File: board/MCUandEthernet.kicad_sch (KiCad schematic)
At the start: 3 parts, among them J1 RJ45_LED_Shielded, U15 Teensy4.1_DEV-16771

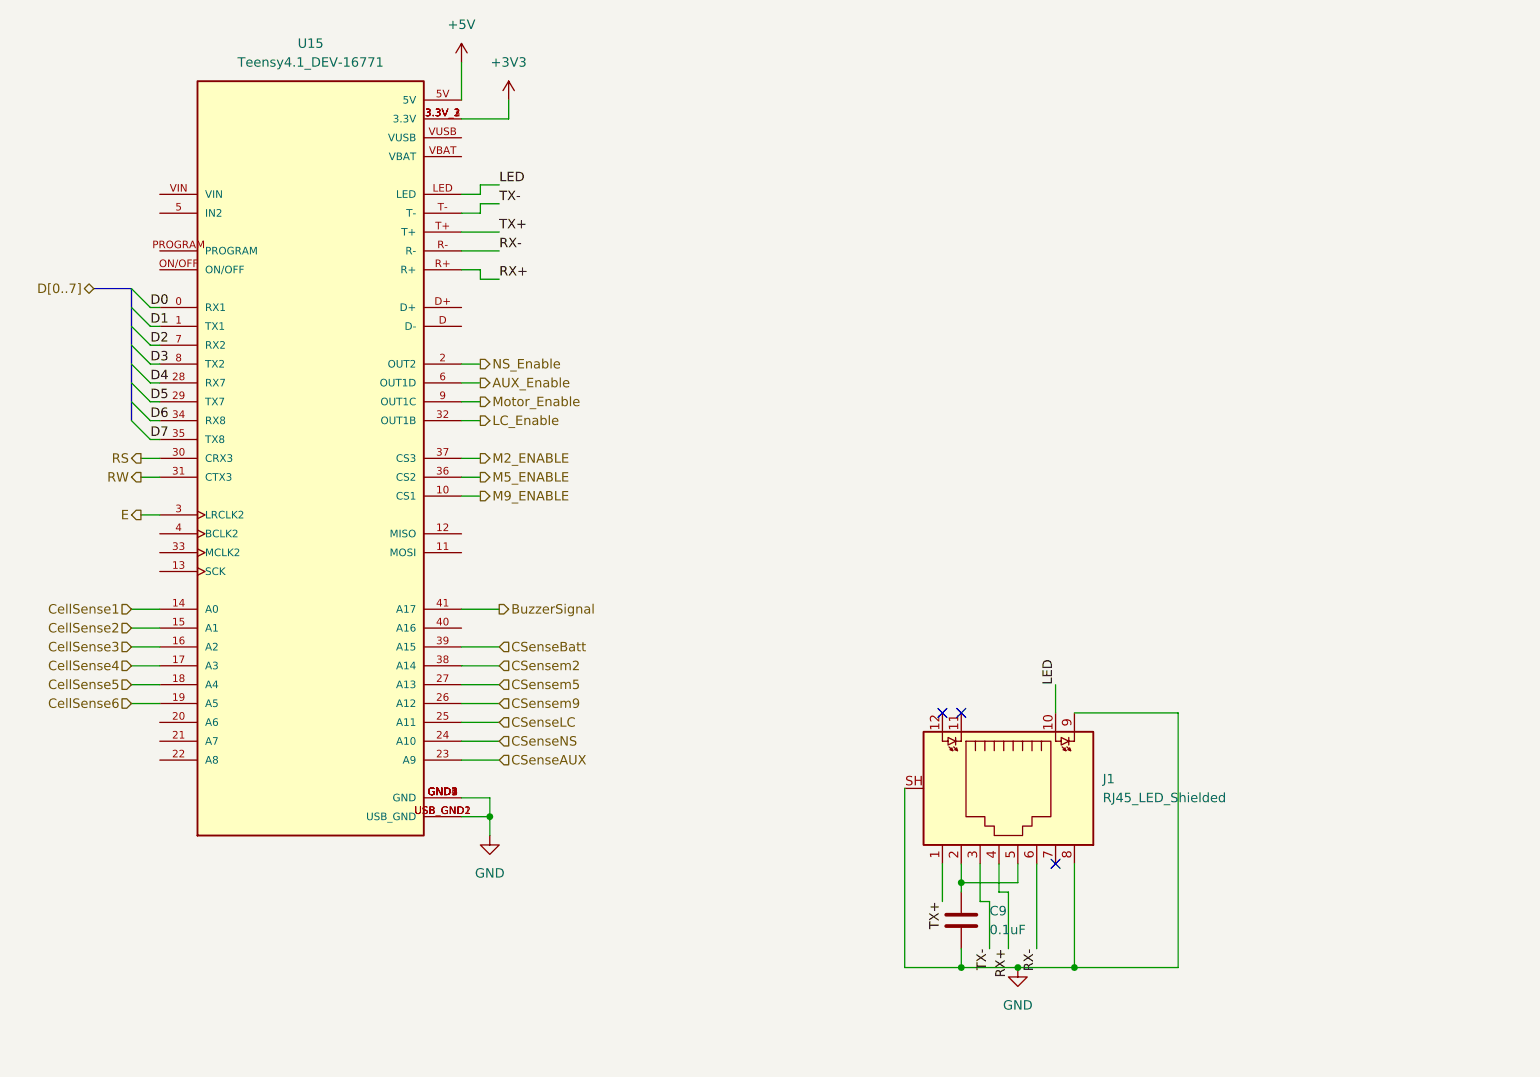
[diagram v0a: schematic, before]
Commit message: added fixes for schematic
redid op amp symbols
put Xs on teensy
Put andersons on current protection page
changed resistor value for buzzer
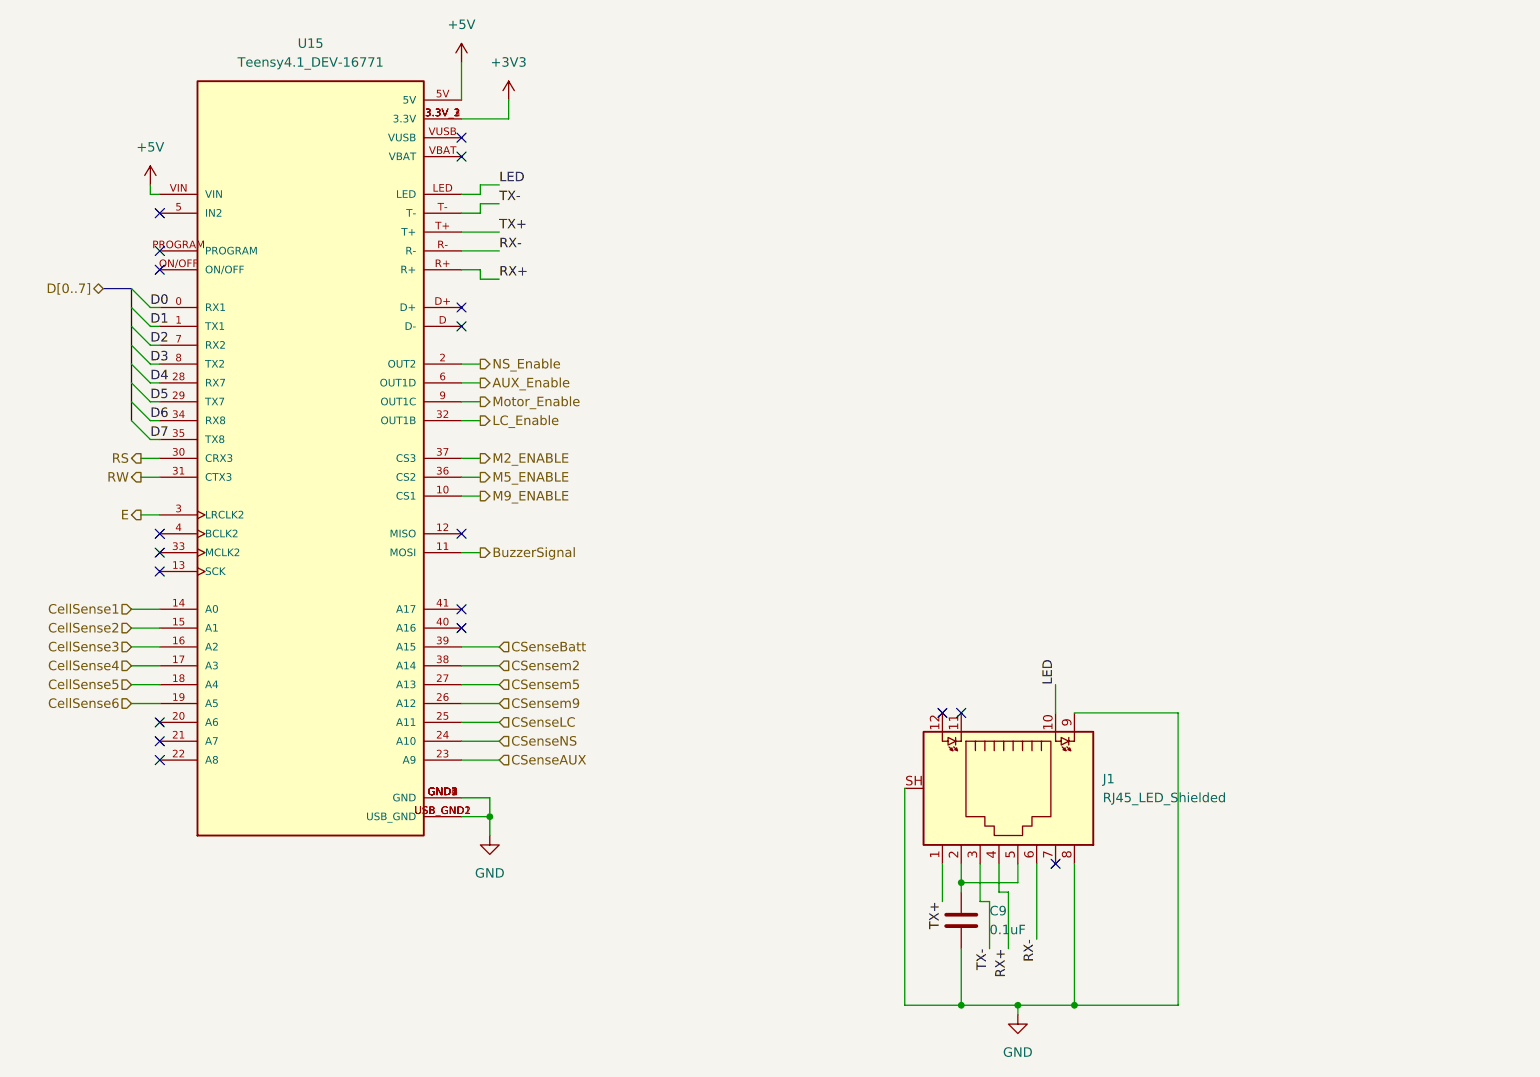
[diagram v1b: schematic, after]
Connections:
- net +5V: now also U15.VIN
- net BuzzerSignal: now also U15.11 (MOSI); no longer U15.41 (A17)
- no-connect marks 3 -> 19
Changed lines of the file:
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@@
 	)
 	(junction
-		(at 135.89 162.56)
+		(at 151.13 167.64)
+		(diameter 0)
+		(color 0 0 0 0)
+	)
+	(junction
+		(at 143.51 167.64)
 		(diameter 0)
 		(color 0 0 0 0)
@@
 	)
 	(junction
-		(at 151.13 162.56)
+		(at 135.89 167.64)
 		(diameter 0)
 		(color 0 0 0 0)
 	)
-	(junction
-		(at 143.51 162.56)
-		(diameter 0)
-		(color 0 0 0 0)
-	)
 	(no_connect
 		(at 133.35 128.27)
 	)
 	(no_connect
+		(at 27.94 68.58)
+	)
+	(no_connect
+		(at 27.94 129.54)
+	)
+	(no_connect
+		(at 68.58 114.3)
+	)
+	(no_connect
+		(at 27.94 134.62)
+	)
+	(no_connect
+		(at 68.58 104.14)
+	)
+	(no_connect
 		(at 148.59 148.59)
 	)
 	(no_connect
+		(at 27.94 106.68)
+	)
+	(no_connect
+		(at 27.94 109.22)
+	)
+	(no_connect
+		(at 27.94 60.96)
+	)
+	(no_connect
+		(at 27.94 104.14)
+	)
+	(no_connect
+		(at 68.58 50.8)
+	)
+	(no_connect
 		(at 135.89 128.27)
+	)
+	(no_connect
+		(at 68.58 76.2)
+	)
+	(no_connect
+		(at 68.58 116.84)
+	)
+	(no_connect
+		(at 68.58 73.66)
+	)
+	(no_connect
+		(at 27.94 132.08)
+	)
+	(no_connect
+		(at 68.58 53.34)
+	)
+	(no_connect
+		(at 27.94 66.04)
 	)
 	(bus_entry
@@
 	(wire
 		(pts
-			(xy 128.27 162.56) (xy 135.89 162.56)
-		)
-		(stroke
-			(width 0)
-			(type default)
-		)
-	)
-	(wire
-		(pts
-			(xy 151.13 148.59) (xy 151.13 162.56)
+			(xy 128.27 167.64) (xy 135.89 167.64)
 		)
 		(stroke
@@
 	(wire
 		(pts
-			(xy 165.1 128.27) (xy 165.1 162.56)
+			(xy 165.1 128.27) (xy 165.1 167.64)
 		)
 		(stroke
@@
 	(wire
 		(pts
+			(xy 26.67 58.42) (xy 27.94 58.42)
+		)
+		(stroke
+			(width 0)
+			(type default)
+		)
+	)
+	(wire
+		(pts
 			(xy 26.67 88.9) (xy 27.94 88.9)
 		)
@@
 	(wire
 		(pts
+			(xy 151.13 148.59) (xy 151.13 167.64)
+		)
+		(stroke
+			(width 0)
+			(type default)
+		)
+	)
+	(wire
+		(pts
 			(xy 24.13 127) (xy 27.94 127)
 		)
@@
 	(wire
 		(pts
-			(xy 68.58 114.3) (xy 73.66 114.3)
-		)
-		(stroke
-			(width 0)
-			(type default)
-		)
-	)
-	(wire
-		(pts
-			(xy 165.1 162.56) (xy 151.13 162.56)
+			(xy 165.1 167.64) (xy 151.13 167.64)
 		)
 		(stroke
@@
 	(wire
 		(pts
+			(xy 143.51 168.91) (xy 143.51 167.64)
+		)
+		(stroke
+			(width 0)
+			(type default)
+		)
+	)
+	(wire
+		(pts
 			(xy 138.43 153.67) (xy 138.43 148.59)
 		)
@@
 	(bus
 		(pts
-			(xy 19.05 71.12) (xy 24.13 71.12)
+			(xy 20.32 71.12) (xy 24.13 71.12)
+		)
+		(stroke
+			(width 0)
+			(type default)
+		)
+	)
+	(wire
+		(pts
+			(xy 26.67 57.15) (xy 26.67 58.42)
 		)
 		(stroke
@@
 	(wire
 		(pts
-			(xy 135.89 162.56) (xy 143.51 162.56)
+			(xy 135.89 167.64) (xy 143.51 167.64)
 		)
 		(stroke
@@
 	(wire
 		(pts
-			(xy 128.27 138.43) (xy 128.27 162.56)
+			(xy 128.27 138.43) (xy 128.27 167.64)
 		)
 		(stroke
@@
 	(wire
 		(pts
-			(xy 146.05 148.59) (xy 146.05 160.02)
+			(xy 146.05 148.59) (xy 146.05 158.75)
 		)
 		(stroke
@@
 	(wire
 		(pts
-			(xy 151.13 162.56) (xy 143.51 162.56)
+			(xy 151.13 167.64) (xy 143.51 167.64)
 		)
 		(stroke
@@
 	(wire
 		(pts
+			(xy 71.12 106.68) (xy 68.58 106.68)
+		)
+		(stroke
+			(width 0)
+			(type default)
+		)
+	)
+	(wire
+		(pts
 			(xy 71.12 93.98) (xy 68.58 93.98)
 		)
@@
 	(wire
 		(pts
-			(xy 135.89 160.02) (xy 135.89 162.56)
+			(xy 135.89 160.02) (xy 135.89 167.64)
 		)
 		(stroke
@@
 	)
 	(label "RX-"
-		(at 146.05 160.02 270)
+		(at 146.05 158.75 270)
 		(effects
 			(font
@@
 	(hierarchical_label "BuzzerSignal"
 		(shape output)
-		(at 73.66 114.3 0)
+		(at 71.12 106.68 0)
 		(effects
 			(font
@@
 	(hierarchical_label "D[0..7]"
 		(shape bidirectional)
-		(at 19.05 71.12 180)
+		(at 20.32 71.12 180)
 		(effects
 			(font
@@
 			)
 			(justify left)
+		)
+	)
+	(symbol
+		(lib_id "power:+5V")
+		(at 26.67 57.15 0)
+		(unit 1)
+		(exclude_from_sim no)
+		(in_bom yes)
+		(on_board yes)
+		(dnp no)
+		(fields_autoplaced yes)
+		(property "Reference" "#PWR091"
+			(at 26.67 60.96 0)
+			(effects
+				(font
+					(size 1.27 1.27)
+				)
+				(hide yes)
+			)
+		)
+		(property "Value" "+5V"
+			(at 26.67 52.07 0)
+			(effects
+				(font
+					(size 1.27 1.27)
+				)
+			)
+		)
+		(property "Footprint" ""
+			(at 26.67 57.15 0)
+			(effects
+				(font
+					(size 1.27 1.27)
+				)
+				(hide yes)
+			)
+		)
+		(property "Datasheet" ""
+			(at 26.67 57.15 0)
+			(effects
+				(font
+					(size 1.27 1.27)
+				)
+				(hide yes)
+			)
+		)
+		(property "Description" "Power symbol creates a global label with name \"+5V\""
+			(at 26.67 57.15 0)
+			(effects
+				(font
+					(size 1.27 1.27)
+				)
+				(hide yes)
+			)
+		)
+		(pin "1"
+		)
+		(instances
+			(project "PowerManagementBoard"
+				(path "/7eaa639d-7062-45e7-be05-1c2855431307/4dc475e3-8611-4a67-a903-307f734d4f8b"
+					(reference "#PWR091")
+					(unit 1)
+				)
+			)
 		)
 	)
@@
 	(symbol
 		(lib_id "power:GND")
-		(at 143.51 162.56 0)
+		(at 143.51 168.91 0)
 		(unit 1)
 		(exclude_from_sim no)
@@
 		(fields_autoplaced yes)
 		(property "Reference" "#PWR041"
+			(at 143.51 175.26 0)
+			(effects
+				(font
+					(size 1.27 1.27)
+				)
+				(hide yes)
+			)
+		)
+		(property "Value" "GND"
+			(at 143.51 173.99 0)
+			(effects
+				(font
+					(size 1.27 1.27)
+				)
+			)
+		)
+		(property "Footprint" ""
 			(at 143.51 168.91 0)
 			(effects
@@
 			)
 		)
-		(property "Value" "GND"
-			(at 143.51 167.64 0)
+		(property "Datasheet" ""
+			(at 143.51 168.91 0)
 			(effects
 				(font
 					(size 1.27 1.27)
 				)
-			)
-		)
-		(property "Footprint" ""
-			(at 143.51 162.56 0)
+				(hide yes)
+			)
+		)
+		(property "Description" "Power symbol creates a global label with name \"GND\" , ground"
+			(at 143.51 168.91 0)
 			(effects
 				(font
-					(size 1.27 1.27)
-				)
-				(hide yes)
-			)
-		)
-		(property "Datasheet" ""
-			(at 143.51 162.56 0)
-			(effects
-				(font
-					(size 1.27 1.27)
-				)
-				(hide yes)
-			)
-		)
-		(property "Description" "Power symbol creates a global label with name \"GND\" , ground"
-			(at 143.51 162.56 0)
-			(effects
-				(font

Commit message: added most datasheets [Except Buzzer]
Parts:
- J1: footprint (none) -> MRDT_Connectors:RJ45_Teensy
- U15: footprint MODULE_DEV-16771 -> MRDT_Shields:Teensy_4_1_Ethernet
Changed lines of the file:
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@@
 			)
 		)
-		(property "Footprint" ""
+		(property "Footprint" "MRDT_Connectors:RJ45_Teensy"
 			(at 141.605 138.43 90)
 			(effects
@@
 			)
 		)
-		(property "Footprint" "MODULE_DEV-16771"
+		(property "Footprint" "MRDT_Shields:Teensy_4_1_Ethernet"
 			(at 101.6 101.6 0)
 			(effects

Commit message: More footprints added
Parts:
- C9: footprint (none) -> Capacitor_SMD:C_0603_1608Metric
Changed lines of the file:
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@@
 			)
 		)
-		(property "Footprint" ""
+		(property "Footprint" "Capacitor_SMD:C_0603_1608Metric"
 			(at 136.8552 160.02 0)
 			(effects

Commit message: Changed footprints to handsolder version
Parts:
- C9: footprint Capacitor_SMD:C_0603_1608Metric -> Capacitor_SMD:C_0603_1608Metric_Pad1.08x0.95mm_HandSolder
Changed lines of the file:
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@@
 			)
 		)
-		(property "Footprint" "Capacitor_SMD:C_0603_1608Metric"
+		(property "Footprint" "Capacitor_SMD:C_0603_1608Metric_Pad1.08x0.95mm_HandSolder"
 			(at 136.8552 160.02 0)
 			(effects

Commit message: experimented with layout
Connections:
- net M5_ENABLE is gone; now on net M9_ENABLE: U15.36 (CS2)
- net M9_ENABLE: no longer U15.10 (CS1)
- net +3V3: no longer names the net of U15.3.3V_1 (3.3V), U15.3.3V_2 (3.3V), U15.3.3V_3 (3.3V)
- net CSensem5: no longer names the net of U15.27 (A13)
- no-connect marks 19 -> 22
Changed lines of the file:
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@@
+	)
+	(no_connect
+		(at 68.58 99.06)
 	)
 	(no_connect
@@
 	)
 	(no_connect
+		(at 68.58 124.46)
+	)
+	(no_connect
 		(at 68.58 116.84)
+	)
+	(no_connect
+		(at 68.58 48.26)
 	)
 	(no_connect
@@
 	(wire
 		(pts
-			(xy 74.93 45.72) (xy 74.93 48.26)
-		)
-		(stroke
-			(width 0)
-			(type default)
-		)
-	)
-	(wire
-		(pts
 			(xy 71.12 58.42) (xy 68.58 58.42)
 		)
@@
 	(wire
 		(pts
-			(xy 68.58 99.06) (xy 71.12 99.06)
+			(xy 68.58 96.52) (xy 71.12 96.52)
 		)
 		(stroke
@@
 	(wire
 		(pts
-			(xy 68.58 124.46) (xy 73.66 124.46)
-		)
-		(stroke
-			(width 0)
-			(type default)
-		)
-	)
-	(wire
-		(pts
 			(xy 68.58 63.5) (xy 73.66 63.5)
 		)
@@
 	(wire
 		(pts
-			(xy 68.58 96.52) (xy 71.12 96.52)
-		)
-		(stroke
-			(width 0)
-			(type default)
-		)
-	)
-	(wire
-		(pts
 			(xy 128.27 138.43) (xy 128.27 167.64)
-		)
-		(stroke
-			(width 0)
-			(type default)
-		)
-	)
-	(wire
-		(pts
-			(xy 74.93 48.26) (xy 68.58 48.26)
 		)
 		(stroke
@@
 		)
 	)
-	(hierarchical_label "M5_ENABLE"
-		(shape output)
-		(at 71.12 96.52 0)
-		(effects
-			(font
-				(size 1.27 1.27)
-			)
-			(justify left)
-		)
-	)
 	(hierarchical_label "E"
 		(shape output)
@@
 	(hierarchical_label "M9_ENABLE"
 		(shape output)
-		(at 71.12 99.06 0)
+		(at 71.12 96.52 0)
 		(effects
 			(font
@@
 			)
 			(justify right)
-		)
-	)
-	(hierarchical_label "CSensem5"
-		(shape input)
-		(at 73.66 124.46 0)
-		(effects
-			(font
-				(size 1.27 1.27)
-			)
-			(justify left)
 		)
 	)
@@
 					(unit 1)
 				)
-			)
-		)
-	)
-	(symbol
-		(lib_id "power:+3V3")
-		(at 74.93 45.72 0)
-		(unit 1)
-		(exclude_from_sim no)
-		(in_bom yes)
-		(on_board yes)
-		(dnp no)
-		(fields_autoplaced yes)
-		(property "Reference" "#PWR040"
-			(at 74.93 49.53 0)
-			(effects
-				(font
-					(size 1.27 1.27)
-				)
-				(hide yes)
-			)
-		)
-		(property "Value" "+3V3"
-			(at 74.93 40.64 0)
-			(effects
-				(font
-					(size 1.27 1.27)
-				)
-			)
-		)
-		(property "Footprint" ""
-			(at 74.93 45.72 0)
-			(effects
-				(font
-					(size 1.27 1.27)
-				)
-				(hide yes)
-			)
-		)
-		(property "Datasheet" ""
-			(at 74.93 45.72 0)
-			(effects
-				(font
-					(size 1.27 1.27)
-				)
-				(hide yes)
-			)
-		)
-		(property "Description" "Power symbol creates a global label with name \"+3V3\""
-			(at 74.93 45.72 0)
-			(effects
-				(font
-					(size 1.27 1.27)
-				)
-				(hide yes)
-			)
-		)
-		(pin "1"
-		)
-		(instances
-			(project ""
-				(path "/7eaa639d-7062-45e7-be05-1c2855431307/4dc475e3-8611-4a67-a903-307f734d4f8b"
-					(reference "#PWR040")
-					(unit 1)
-				)

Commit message: 17 hours of our lives
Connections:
- net RS: now also U15.21 (A7); no longer U15.30 (CRX3)
- net RW: now also U15.22 (A8); no longer U15.31 (CTX3)
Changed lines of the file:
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@@
+	)
+	(no_connect
+		(at 27.94 96.52)
 	)
 	(no_connect
@@
 	)
 	(no_connect
-		(at 27.94 134.62)
+		(at 27.94 93.98)
 	)
 	(no_connect
@@
 	(no_connect
 		(at 68.58 73.66)
-	)
-	(no_connect
-		(at 27.94 132.08)
 	)
 	(no_connect
@@
 	(wire
 		(pts
+			(xy 25.4 134.62) (xy 27.94 134.62)
+		)
+		(stroke
+			(width 0)
+			(type default)
+		)
+	)
+	(wire
+		(pts
 			(xy 26.67 73.66) (xy 27.94 73.66)
 		)
@@
 	(wire
 		(pts
-			(xy 25.4 96.52) (xy 27.94 96.52)
+			(xy 25.4 132.08) (xy 27.94 132.08)
 		)
 		(stroke
@@
 		(pts
 			(xy 140.97 152.4) (xy 140.97 148.59)
-		)
-		(stroke
-			(width 0)
-			(type default)
-		)
-	)
-	(wire
-		(pts
-			(xy 25.4 93.98) (xy 27.94 93.98)
 		)
 		(stroke
@@
 	(hierarchical_label "RW"
 		(shape output)
-		(at 25.4 96.52 180)
+		(at 25.4 134.62 180)
 		(effects
 			(font
@@
 	(hierarchical_label "RS"
 		(shape output)
-		(at 25.4 93.98 180)
-		(effects
-			(font
+		(at 25.4 132.08 180)
+		(effects
+			(font
